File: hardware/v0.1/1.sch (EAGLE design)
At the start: 45 parts, among them IC2 STM32F10XCXT6, U1 MIC5219 3.3V, Y1 8MHZ, Y2 32768

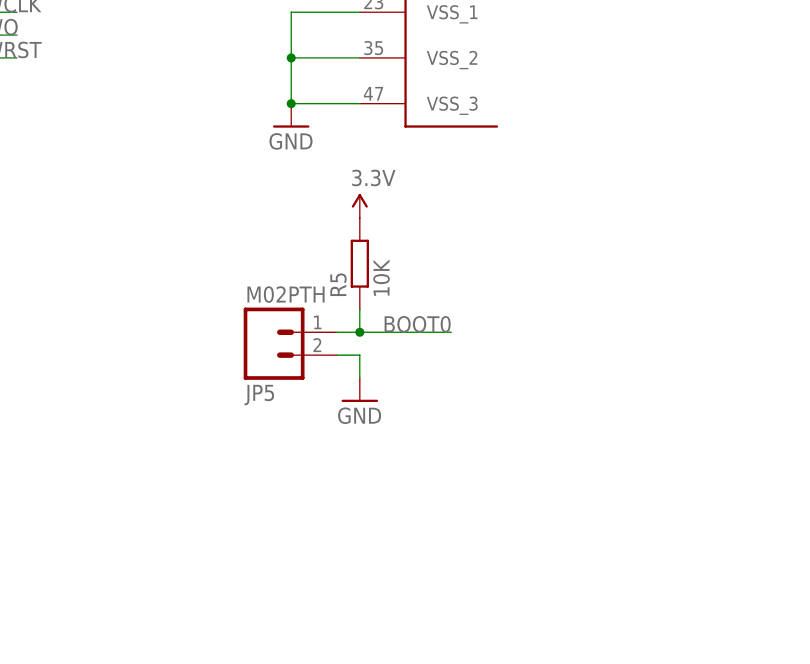
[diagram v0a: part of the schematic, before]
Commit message: Update readme.md, fix a minor bug on PCB
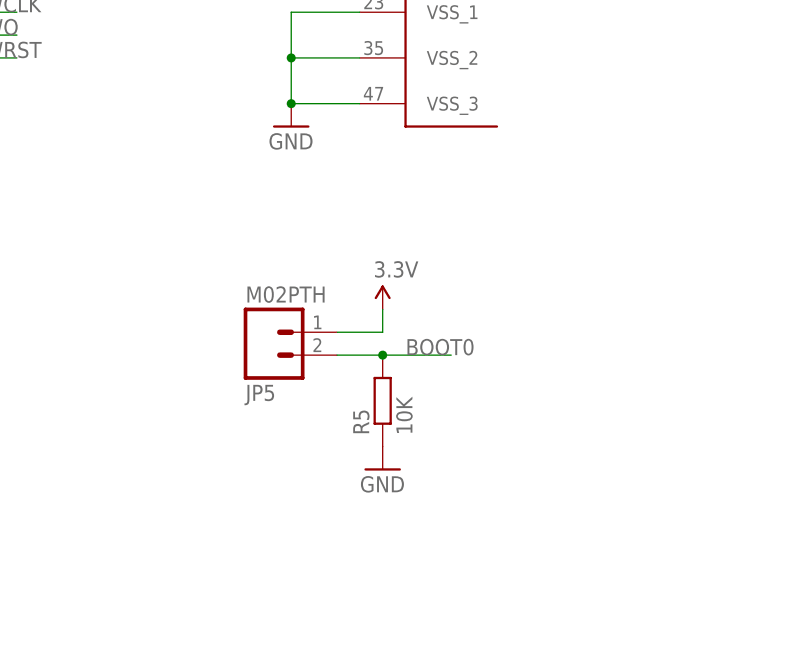
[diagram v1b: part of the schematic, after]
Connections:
- net 3.3V: now also JP5.1; no longer R5.2
- net BOOT0: now also JP5.2, R5.2; no longer JP5.1, R5.1
- net GND: now also R5.1; no longer JP5.2
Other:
- moved on the sheet: R5
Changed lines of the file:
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@@
 <part name="GND8" library="SparkFun-Aesthetics" deviceset="GND" device=""/>
 <part name="GND9" library="SparkFun-Aesthetics" deviceset="GND" device=""/>
-<part name="SUPPLY4" library="SparkFun-Aesthetics" deviceset="3.3V" device=""/>
 <part name="R5" library="rcl" deviceset="R-EU_" device="R0603" value="10K"/>
 <part name="Y1" library="SparkFun-FreqCtrl" deviceset="CRYSTAL" device="5X3" value="8MHZ"/>
@@
 <part name="SUPPLY12" library="SparkFun-Aesthetics" deviceset="3.3V" device=""/>
 <part name="GND17" library="SparkFun-Aesthetics" deviceset="GND" device=""/>
+<part name="SUPPLY4" library="SparkFun-Aesthetics" deviceset="3.3V" device=""/>
 </parts>
 <sheets>
@@
 <instance part="SUPPLY7" gate="G$1" x="-15.24" y="-2.54"/>
 <instance part="GND8" gate="1" x="-15.24" y="-33.02"/>
-<instance part="GND9" gate="1" x="45.72" y="-63.5"/>
-<instance part="SUPPLY4" gate="G$1" x="45.72" y="-43.18"/>
-<instance part="R5" gate="G$1" x="45.72" y="-48.26" rot="R90"/>
+<instance part="GND9" gate="1" x="48.26" y="-71.12"/>
+<instance part="R5" gate="G$1" x="48.26" y="-63.5" rot="R90"/>
 <instance part="Y1" gate="G$1" x="203.2" y="35.56" rot="R270"/>
 <instance part="C6" gate="G$1" x="210.82" y="40.64" rot="R90"/>
@@
 <instance part="SUPPLY12" gate="G$1" x="-5.08" y="-71.12"/>
 <instance part="GND17" gate="1" x="-5.08" y="-88.9"/>
+<instance part="SUPPLY4" gate="G$1" x="48.26" y="-53.34"/>
 </instances>
 <busses>
@@
 </segment>
 <segment>
-<pinref part="JP5" gate="G$1" pin="2"/>
-<wire x1="43.18" y1="-58.42" x2="45.72" y2="-58.42" width="0.1524" layer="91"/>
-<pinref part="GND9" gate="1" pin="GND"/>
-<wire x1="45.72" y1="-58.42" x2="45.72" y2="-60.96" width="0.1524" layer="91"/>
-</segment>
-<segment>
 <pinref part="GND15" gate="1" pin="GND"/>
 <wire x1="213.36" y1="12.7" x2="213.36" y2="15.24" width="0.1524" layer="91"/>
@@
 <wire x1="-17.78" y1="-86.36" x2="-5.08" y2="-86.36" width="0.1524" layer="91"/>
 <pinref part="GND17" gate="1" pin="GND"/>
+</segment>
+<segment>
+<pinref part="R5" gate="G$1" pin="1"/>
+<pinref part="GND9" gate="1" pin="GND"/>
 </segment>
 </net>
@@
 <wire x1="45.72" y1="-5.08" x2="38.1" y2="-5.08" width="0.1524" layer="91"/>
 <junction x="38.1" y="-5.08"/>
-</segment>
-<segment>
-<pinref part="SUPPLY4" gate="G$1" pin="3.3V"/>
-<pinref part="R5" gate="G$1" pin="2"/>
 </segment>
 <segment>
@@
 <pinref part="SUPPLY12" gate="G$1" pin="3.3V"/>
 </segment>
+<segment>
+<pinref part="JP5" gate="G$1" pin="1"/>
+<wire x1="43.18" y1="-55.88" x2="48.26" y2="-55.88" width="0.1524" layer="91"/>
+<pinref part="SUPPLY4" gate="G$1" pin="3.3V"/>
+<wire x1="48.26" y1="-55.88" x2="48.26" y2="-53.34" width="0.1524" layer="91"/>
+</segment>
 </net>
 <net name="N$1" class="0">
@@
 <net name="BOOT0" class="0">
 <segment>
-<pinref part="JP5" gate="G$1" pin="1"/>
-<wire x1="43.18" y1="-55.88" x2="45.72" y2="-55.88" width="0.1524" layer="91"/>
-<pinref part="R5" gate="G$1" pin="1"/>
-<wire x1="45.72" y1="-55.88" x2="45.72" y2="-53.34" width="0.1524" layer="91"/>
-<junction x="45.72" y="-55.88"/>
-<wire x1="45.72" y1="-55.88" x2="55.88" y2="-55.88" width="0.1524" layer="91"/>
-<label x="48.26" y="-55.88" size="1.778" layer="95"/>
-</segment>
-<segment>
 <pinref part="IC2" gate="RESET" pin="BOOT0"/>
 <wire x1="187.96" y1="73.66" x2="200.66" y2="73.66" width="0.1524" layer="91"/>
 <label x="190.5" y="73.66" size="1.778" layer="95"/>
 </segment>
-</net>
+<segment>
+<pinref part="JP5" gate="G$1" pin="2"/>
+<pinref part="R5" gate="G$1" pin="2"/>
+<wire x1="48.26" y1="-58.42" x2="43.18" y2="-58.42" width="0.1524" layer="91"/>
+<wire x1="48.26" y1="-58.42" x2="55.88" y2="-58.42" width="0.1524" layer="91"/>
+<junction x="48.26" y="-58.42"/>
+<label x="50.8" y="-58.42" size="1.778" layer="95"/>
+</segment>
+</net>
